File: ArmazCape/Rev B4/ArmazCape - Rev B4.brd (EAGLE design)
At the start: 85 x 70.5 mm, 169 parts, among them IC1 AT93C46EN-SH-BSOIC8, P1 RB1-125BAG1A, Q1 32.768kHz, 12.5pF, Q4 IRLML6344TRPBF, Q5 IRLML6344TRPBF, U1 L7985A, U2 L7985A, U3 DS1307ZN+, U4 24AA256-I/SN, U5 CD4050BD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

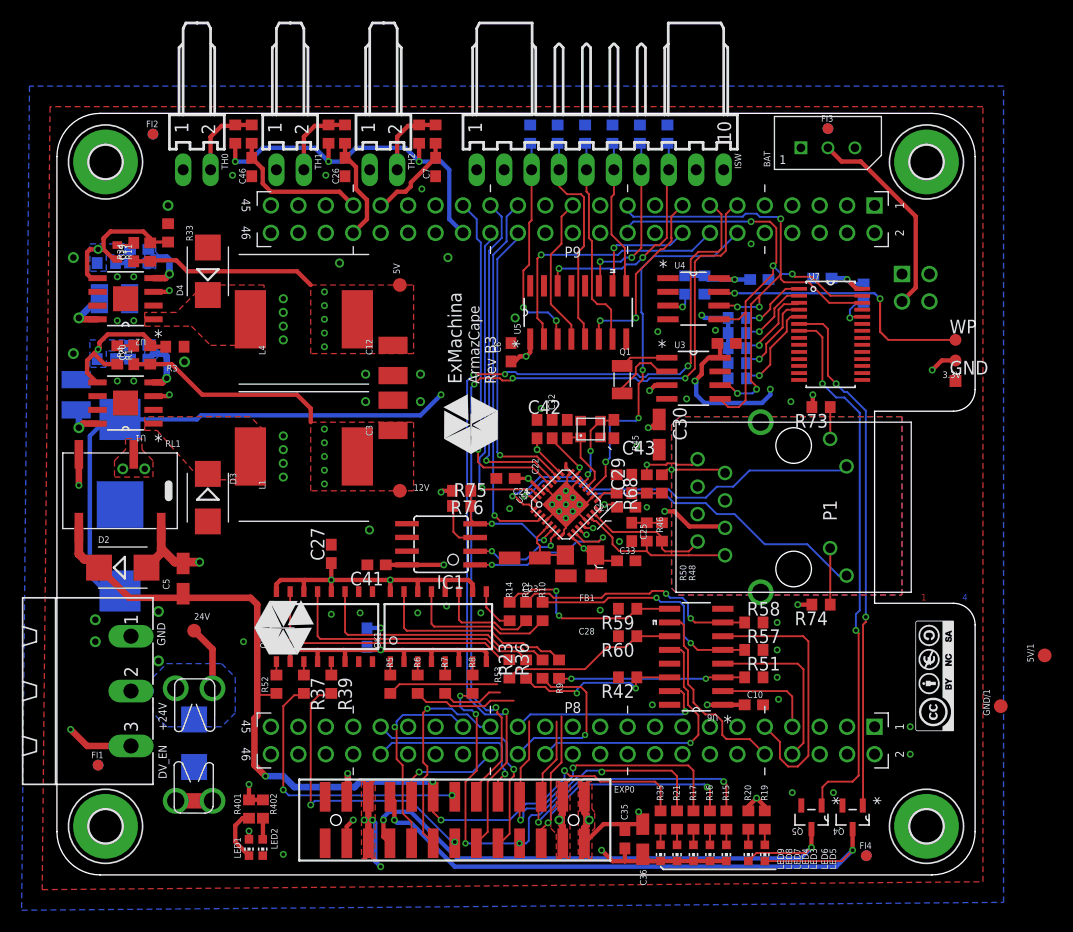
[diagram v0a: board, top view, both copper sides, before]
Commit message: ArmazCape - Rev B4: Reorganized schematics layout
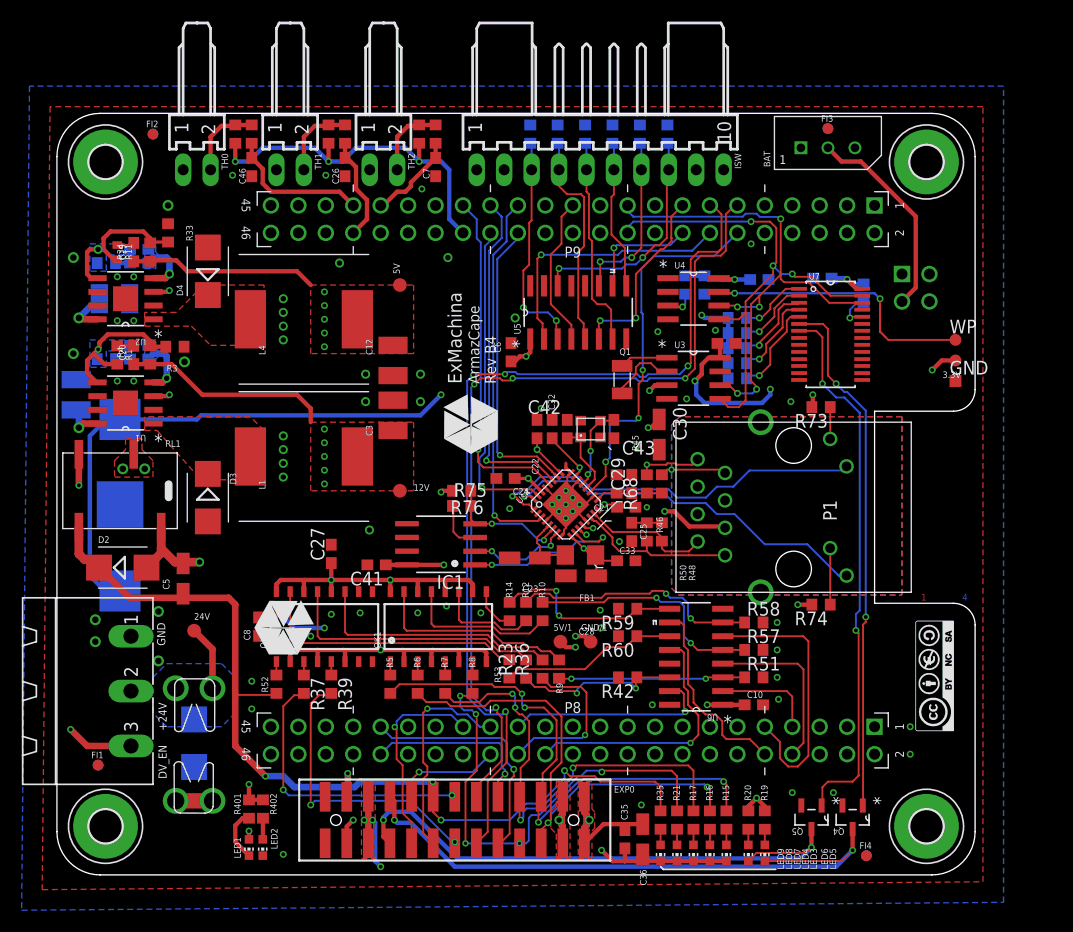
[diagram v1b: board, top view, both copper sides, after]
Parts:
- BAT: device con-molex:5267-02A -> con-molex:5267-03A
- moved 5V/1 44.8 mm to (46.6, 21.6), turned to 90 degrees
- moved GND/1 38.4 mm to (49.4, 21.6), turned to 270 degrees
- moved C8 10.1 mm to (18.7, 23.0), flipped to the top
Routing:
- net ESW0: track 42.0 -> 49.6 mm, vias 2 -> 4
- net +5V/1: track 20.8 -> 27.8 mm, vias 2 -> 4
- net ESW1: track 41.0 -> 46.1 mm
- net ESW2: track 38.1 -> 42.5 mm, vias 2 -> 4
- net GND1: track 73.5 -> 77.8 mm, vias 4 -> 5
- net GND: vias 71 -> 73
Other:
- board text added: "ArmazCape Rev B4"
- board text added: "ExMachina Released under Creatives Commons CC BY-NC-SA"
- board text added: "www.exmachina.fr"
- board text removed: "ArmazCape Rev B3"
- board text removed: "ExMachina Released under Creatives Commons CC BY-SA"

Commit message: Update attributes in ArmazCape - Rev B4
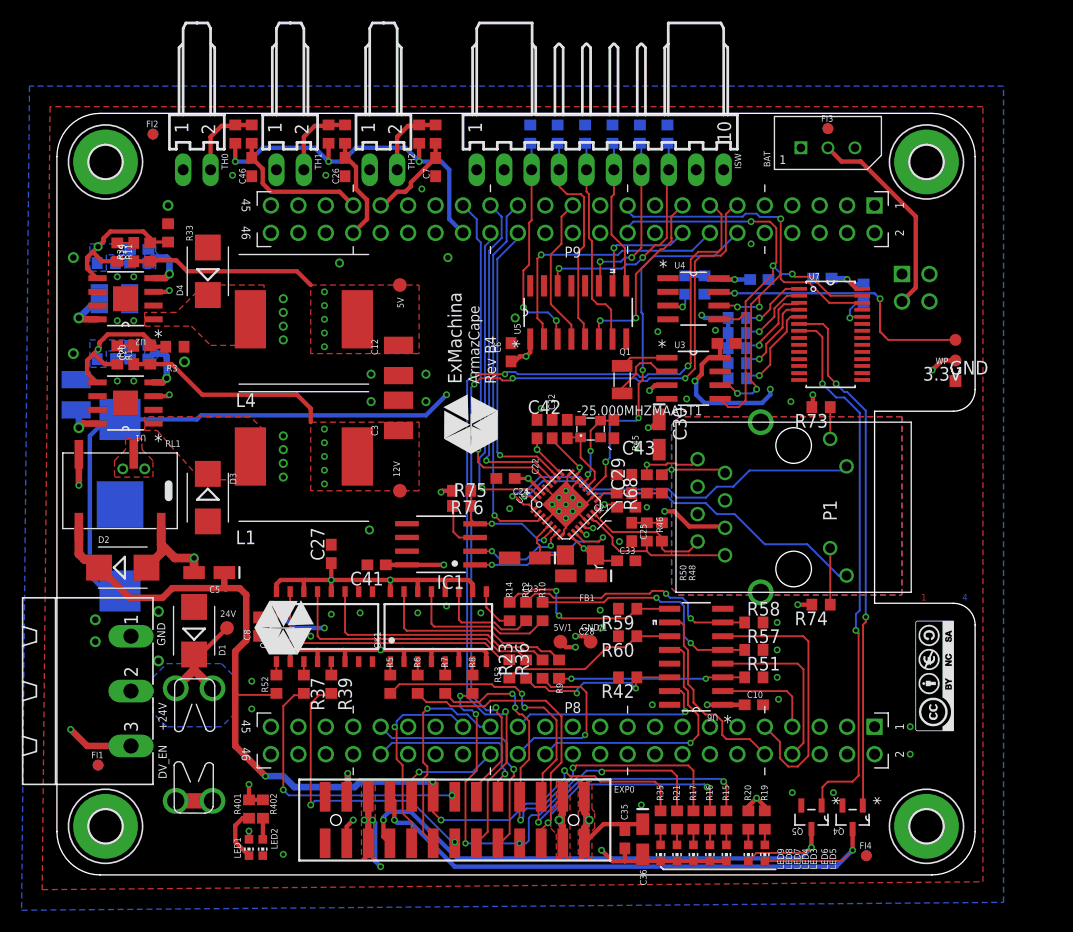
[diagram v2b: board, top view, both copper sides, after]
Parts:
- R11: device rcl:R0402 -> rcl:R0603
- R13, R18, R31: value 4K7, 1% -> 4K7
- R15, R16, R17, R21: value 1.5K -> 1K5
- R19, R20, R22, R25, R26, R27, R28, R29, R30, R401, R402, R41, R76: value 4.7K -> 4K7
- moved D1 10.4 mm to (12.7, 22.6), flipped to the top, turned to 90 degrees
- moved 24V 3.06 mm to (15.7, 22.9)
- moved C5 2.48 mm to (14.1, 28.0), turned to 180 degrees
- moved C12 0.51 mm to (31.6, 47.6)
- moved C3 0.51 mm to (31.6, 42.5)
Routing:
- net VDD_IN: track 31.7 -> 36.0 mm
- net DV0: track 85.8 -> 89.5 mm
- net GND1: track 77.8 -> 79.0 mm
- net GND: track 18.0 -> 16.9 mm

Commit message: Reroute UART isolation
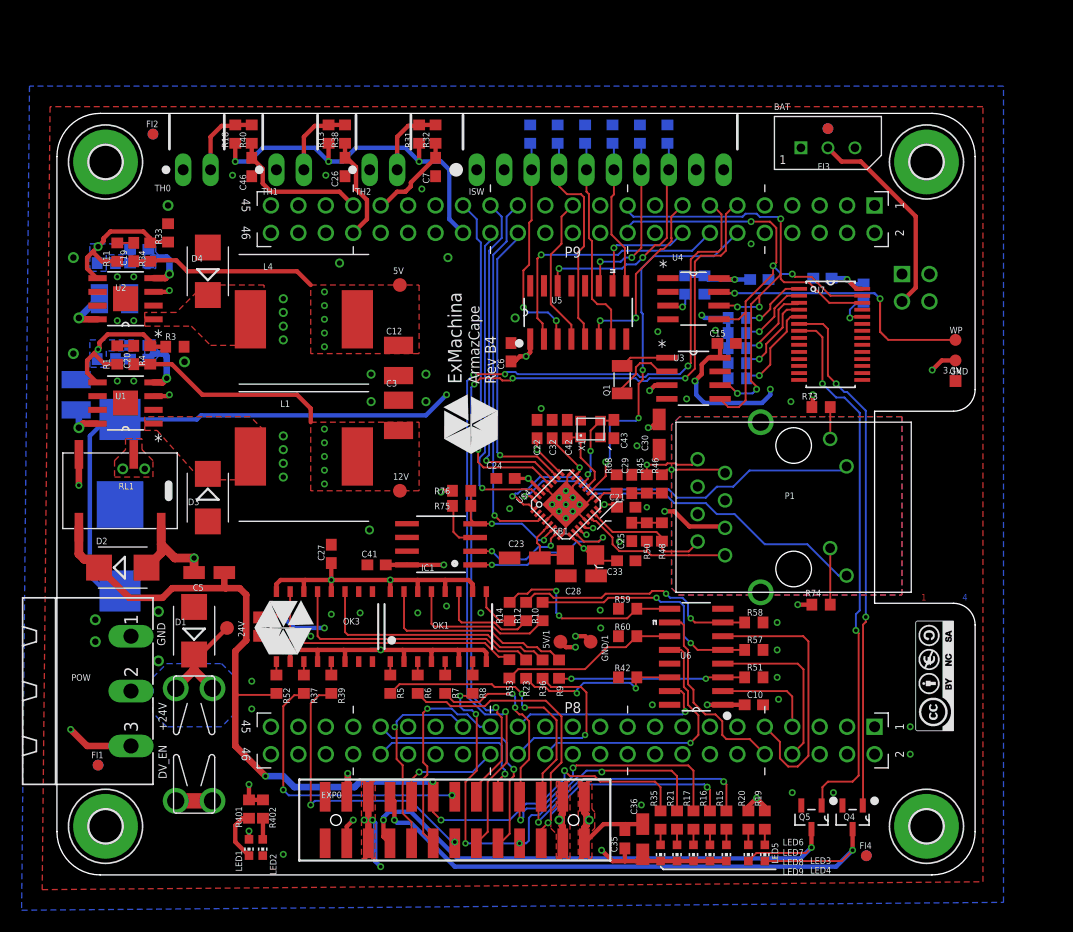
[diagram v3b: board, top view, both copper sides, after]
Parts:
- X1: value 8Z-25.000MHZMAAJ-T -> 8Z-25.000MAAJ-T
- renumbered -25.000MHZMAAJ-T1 to X1
